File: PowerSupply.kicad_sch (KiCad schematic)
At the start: 15 parts, among them U4 UM1750S-00

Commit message: sebelum pemeriksaan terkahir
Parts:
- removed R23: 200K, symbol Device:R_US
- removed U4: UM1750S-00, symbol qris_iot:UM1750S-00
- added C18, C46, C47, C50, C51, C55, C56, C62: 0.22uF, symbol Device:C_Polarized_US
- added C19, C66, C67: 0.1UF, symbol Device:C_Polarized_US
- added C43: 10uF, symbol Device:C_Polarized_US
- added C44, C45, C48: 22uF, symbol Device:C_Polarized_US
- added C49, C54, C61: 4.7uF, symbol Device:C_Polarized_US
- added C57: 1.0uF, symbol Device:C_Polarized_US
- added D5, D7: RB521S30, symbol Device:D_Schottky
- added IC1: RCLAMP0854P.TCT, UFDFN06_1P6X1P6_SEM, symbol tvs:RCLAMP0854P.TCT
- added J8: USB_B_Micro, symbol Connector:USB_B_Micro
- added L2, L3: 330 ohm, symbol Device:L_Ferrite
- added L4: 900 OHM, symbol Device:L_Coupled_1243
- added R48, R50, R51, R63: 0, symbol Device:R_US
- added R6: 10K, symbol Device:R_US
- added R61: 1.5K 1%, symbol Device:R_US
- added R62: R_US, symbol Device:R_US
- added U4: UM803RS, symbol tvs:UM803RS
- C29: value 10UF -> 0.22uF; Value2 10V -> (none)
- C30: value 0.1UF -> 0.22uF; Value2 10V -> (none)
- C31: value 4.7UF -> 0.22uF; Value2 6.3V -> (none)
- C32: value 0.1UF -> 4.7uF; Value2 10V -> 6.3V
- R22: value 464K -> 30K
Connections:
- net DCDC_3V3: now also R51.2, R61.1
- net GND: now also C18.2, C19.2, C43.2, C44.2, C45.2, C46.2, C47.2, C48.2, C49.2, C50.2, C51.2, C54.2, C55.2, C56.2, C57.2, C61.2, C62.2, C66.2, C67.2, IC1.7 (GND), J8.5 (GND), L2.2, U4.1 (GND)
- net VDD_HIGH_IN_3V3: now also C54.1, C55.1
- net VLDO_3V3: now also R50.2; no longer C31.1, C32.1, R22.2
- net DCDC_PSWITCH_MCU: now reaches R22.1
- net DCDC_PSWITCH_MCU: now also C51.1
- net 5V_SYS renamed DCDC_OUT
- net DCDC_OUT: now also C31.1, C32.1, C44.1, C45.1, C46.1
- net MCU_DCDC_IN_3V3 renamed MCU_DCDC_IN
- net MCU_DCDC_IN: now also R22.2, C47.1, C48.1, C49.1, C50.1
- new net: J8.6 (Shield), L2.1
- new net: IC1.3 (USB_ID), J8.4 (ID)
- new net: IC1.6 (VBUS), J8.1 (VBUS), L3.1
- new net: R62.1, U4.2 (~RESET)
- new net: C66.1, R61.2, U4.3 (VCC)
- new net 5V_USB_OTG: C43.1, L3.2, R48.1
- new net 5V_USB_OTG_S: R48.2
- new net DM_FB: IC1.1 (DM), J8.2 (D-), L4.2
- new net DP_FB: IC1.2 (DP), J8.3 (D+), L4.3
- new net OTG1_DN: L4.1
- new net OTG1_DP: L4.4
- new net P3V3_SDA: R63.2
- new net POR_B: C67.1, R62.2
- new net VDDA_2P5_CAP: C61.1, C62.1
- new net VDDA_ADC_3P3_MCU: C56.1, C57.1
- new net VDD_COIN_3V: D7.2 (A), R6.2
- new net VDD_SNVS_3V3: C19.1, D5.2 (A), R50.1, R51.1, R63.1
- new net VDD_SNVS_IN: C18.1, D5.1 (K), D7.1 (K), R6.1
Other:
- note removed: "3V3 LDO for SNVS"

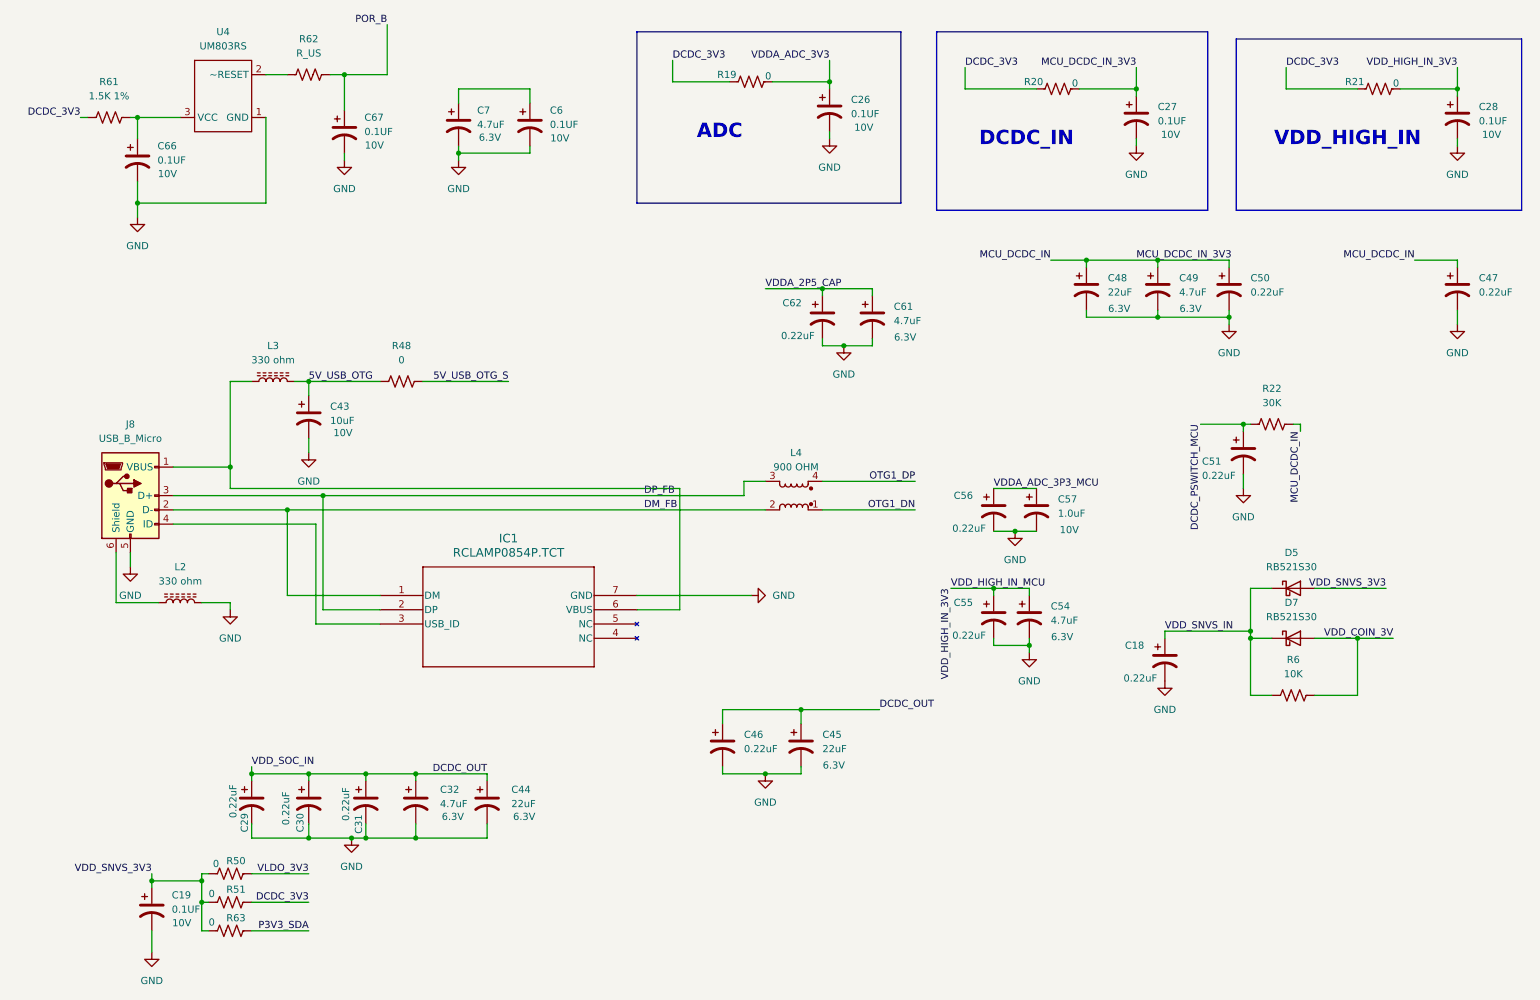
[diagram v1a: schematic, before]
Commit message: Add power usb
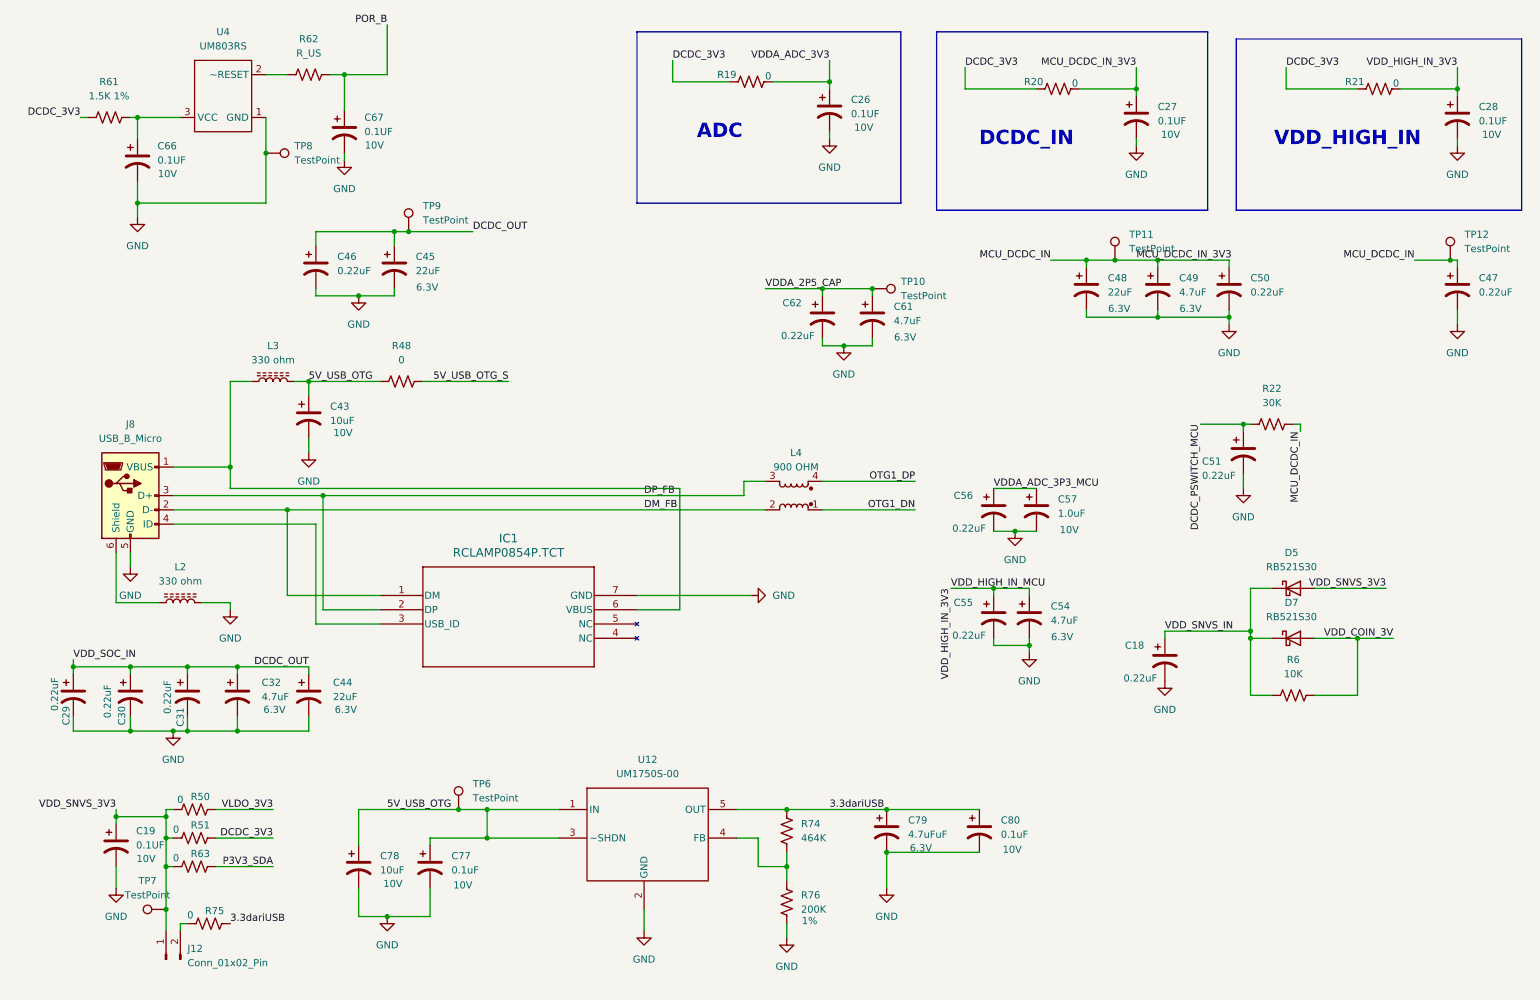
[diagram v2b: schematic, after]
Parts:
- removed C6: 0.1UF, symbol Device:C_Polarized_US
- removed C7: 4.7uF, symbol Device:C_Polarized_US
- added C77, C80: 0.1uF, symbol Device:C_Polarized_US
- added C78: 10uF, symbol Device:C_Polarized_US
- added C79: 4.7uFuF, symbol Device:C_Polarized_US
- added J12: Conn_01x02_Pin, symbol Connector:Conn_01x02_Pin
- added R74: 464K, symbol Device:R_US
- added R75: 0, symbol Device:R_US
- added R76: 200K, symbol Device:R_US
- added TP10, TP11, TP12, TP6, TP7, TP8, TP9: TestPoint, symbol Connector:TestPoint
- added U12: UM1750S-00, symbol qris_iot:UM1750S-00
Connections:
- net 5V_USB_OTG: now also C77.1, C78.1, TP6.1, U12.1 (IN), U12.3 (~SHDN)
- net DCDC_OUT: now also TP9.1
- net GND: now also C77.2, C78.2, C79.2, C80.2, R76.2, TP8.1, U12.2 (GND)
- net MCU_DCDC_IN: now also TP11.1, TP12.1
- net VDDA_2P5_CAP: now also TP10.1
- net VDD_SNVS_3V3: now also J12.1 (Pin_1), TP7.1
- new net: R74.2, R76.1, U12.4 (FB)
- new net: J12.2 (Pin_2), R75.1
- new net 3.3dariUSB: C79.1, C80.1, R74.1, R75.2, U12.5 (OUT)
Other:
- moved on the sheet: C19, C29, C30, C31, C32, C44, C45, C46, R50, R51, R63

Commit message: menambah lebih dari setengah footprint
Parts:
- C18, C29, C30, C31, C46, C47, C50, C51, C55, C56, C62: value 0.22uF -> 0.22UF; footprint (none) -> Capacitor_SMD:C_0402_1005Metric; MANUFACTURER (none) -> CL10A226MQ8NRNE
- C19, C26, C27, C28, C66, C67: footprint (none) -> Capacitor_SMD:C_0402_1005Metric; MANUFACTURER (none) -> CC0402KRX5R6BB104
- C32, C49, C54, C61: value 4.7uF -> 4.7UF; footprint (none) -> Capacitor_SMD:C_0402_1005Metric; MANUFACTURER (none) -> C1005X5R0J475M050BC
- C43, C78: value 10uF -> 10UF; footprint (none) -> Capacitor_SMD:C_0603_1608Metric; MANUFACTURER (none) -> GRM188R61A106KE69D
- C44, C45, C48: value 22uF -> 22UF; footprint (none) -> Capacitor_SMD:C_0603_1608Metric
- C57: value 1.0uF -> 1UF; footprint (none) -> Capacitor_SMD:C_0402_1005Metric
- C77: value 0.1uF -> 0.1UF; MANUFACTURER (none) -> CC0402KRX5R6BB104
- C79: value 4.7uFuF -> 4.7UF; footprint (none) -> Capacitor_SMD:C_0402_1005Metric; MANUFACTURER (none) -> C1005X5R0J475M050BC
- C80: value 0.1uF -> 0.1UF; footprint (none) -> Capacitor_SMD:C_0402_1005Metric; MANUFACTURER (none) -> CC0402KRX5R6BB104
- IC1: footprint UFDFN06_1P6X1P6_SEM -> footprints:UFDFN06_1P6X1P6_SEM
- R19, R20, R21, R22, R48, R50, R51, R6, R61, R63: footprint (none) -> Resistor_SMD:R_0402_1005Metric
- TP10, TP11, TP12, TP6, TP7, TP8, TP9: footprint (none) -> MountingHole:MountingHole_2.1mm

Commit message: menambahkan beberapa component lagi
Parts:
- C77: footprint (none) -> Capacitor_SMD:C_0402_1005Metric
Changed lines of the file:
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@@
 			)
 		)
-		(property "Footprint" ""
+		(property "Footprint" "Capacitor_SMD:C_0402_1005Metric"
 			(at 85.09 167.64 0)
 			(effects

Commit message: da
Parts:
- U12: footprint (none) -> Package_TO_SOT_SMD:SOT-23-5
- U4: footprint (none) -> Package_TO_SOT_SMD:SOT-23-3
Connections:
- net VDD_COIN_3V: now also D5.2 (A); no longer D7.2 (A), R6.2
- net VDD_SNVS_3V3: now also D7.2 (A), R6.2; no longer D5.2 (A)

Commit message: add some revision
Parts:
- added R77: 0, Resistor_SMD:R_0402_1005Metric, symbol Device:R_US
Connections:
- net VDD_SNVS_3V3: now also R77.1
- new net FC41D_3V3: R77.2
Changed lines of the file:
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@@
 	)
 	(junction
+		(at 38.1 172.72)
+		(diameter 0)
+		(color 0 0 0 0)
+	)
+	(junction
 		(at 231.14 125.73)
 		(diameter 0)
@@
 	(wire
 		(pts
+			(xy 39.37 172.72) (xy 38.1 172.72)
+		)
+		(stroke
+			(width 0)
+			(type default)
+		)
+	)
+	(wire
+		(pts
 			(xy 83.82 81.28) (xy 99.06 81.28)
 		)
@@
 	(wire
 		(pts
-			(xy 177.8 118.11) (xy 185.42 118.11)
+			(xy 167.64 118.11) (xy 185.42 118.11)
 		)
 		(stroke
@@
 	(wire
 		(pts
+			(xy 46.99 172.72) (xy 57.15 172.72)
+		)
+		(stroke
+			(width 0)
+			(type default)
+		)
+	)
+	(wire
+		(pts
 			(xy 158.75 74.93) (xy 163.83 74.93)
 		)
@@
 	(wire
 		(pts
-			(xy 38.1 167.64) (xy 38.1 175.26)
+			(xy 38.1 167.64) (xy 38.1 172.72)
 		)
 		(stroke
@@
 	(wire
 		(pts
+			(xy 38.1 172.72) (xy 38.1 175.26)
+		)
+		(stroke
+			(width 0)
+			(type default)
+		)
+	)
+	(wire
+		(pts
 			(xy 180.34 29.21) (xy 193.04 29.21)
 		)
@@
 		)
 	)
-	(label "VDD_HIGH_IN_MCU"
-		(at 177.8 118.11 0)
-		(fields_autoplaced yes)
-		(effects
-			(font
-				(size 1.27 1.27)
-			)
-			(justify left bottom)
-		)
-	)
 	(global_label "VDD_HIGH_IN_3V3"
 		(shape input)
@@
 		)
 	)
+	(global_label "VDD_HIGH_IN_MCU"
+		(shape input)
+		(at 167.64 118.11 270)
+		(fields_autoplaced yes)
+		(effects
+			(font
+				(size 1.27 1.27)
+			)
+			(justify right)
+		)
+		(property "Intersheetrefs" "${INTERSHEET_REFS}"
+			(at 167.64 138.1496 90)
+			(effects
+				(font
+					(size 1.27 1.27)
+				)
+				(justify right)
+				(hide yes)
+			)
+		)
+	)
+	(global_label "FC41D_3V3"
+		(shape input)
+		(at 57.15 172.72 0)
+		(fields_autoplaced yes)
+		(effects
+			(font
+				(size 1.27 1.27)
+			)
+			(justify left)
+		)
+		(property "Intersheetrefs" "${INTERSHEET_REFS}"
+			(at 70.658 172.72 0)
+			(effects
+				(font
+					(size 1.27 1.27)
+				)
+				(justify left)
+				(hide yes)
+			)
+		)
+	)
 	(global_label "MCU_DCDC_IN_3V3"
 		(shape input)
@@
 	(global_label "VDD_HIGH_IN_3V3"
 		(shape input)
-		(at 177.8 118.11 270)
+		(at 172.72 118.11 270)
 		(fields_autoplaced yes)
 		(effects
@@
 		)
 		(property "Intersheetrefs" "${INTERSHEET_REFS}"
-			(at 177.8 137.6053 90)
+			(at 172.72 137.6053 90)
 			(effects
 				(font
@@
 					(unit 1)
 				)
+			)
+		)
+	)
+	(symbol
+		(lib_id "Device:R_US")
+		(at 43.18 172.72 90)
+		(unit 1)
+		(exclude_from_sim no)
+		(in_bom yes)
+		(on_board yes)
+		(dnp no)
+		(property "Reference" "R77"
+			(at 44.196 170.434 90)
+			(effects
+				(font
+					(size 1.27 1.27)
+				)
+			)
+		)
+		(property "Value" "0"
+			(at 39.878 171.196 90)
+			(effects
+				(font
+					(size 1.27 1.27)
+				)
+			)
+		)
+		(property "Footprint" "Resistor_SMD:R_0402_1005Metric"
+			(at 43.434 171.704 90)
+			(effects
+				(font
+					(size 1.27 1.27)
+				)
+				(hide yes)
+			)
+		)
+		(property "Datasheet" "~"
+			(at 43.18 172.72 0)
+			(effects
+				(font
+					(size 1.27 1.27)
+				)
+				(hide yes)
+			)
+		)
+		(property "Description" "Resistor, US symbol"
+			(at 43.18 172.72 0)
+			(effects
+				(font
+					(size 1.27 1.27)
+				)
+				(hide yes)
+			)
+		)
+		(property "DigikeyPartNumber" ""
+			(at 43.18 172.72 0)
+			(effects
+				(font
+					(size 1.27 1.27)
+				)
+				(hide yes)
+			)
+		)
+		(pin "2"
+		)
+		(pin "1"
+		)
+		(instances
+			(project "qris_iot"
+				(path "/7e5ed2de-adc7-481a-a10e-7326381f5ab2/0c446b05-2ff4-4319-859d-c1e217bf307a"
+					(reference "R77")
+					(unit 1)
+				)
